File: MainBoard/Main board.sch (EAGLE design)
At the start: 9 parts

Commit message: Main board
Relabelled everything with power supply, labelled and redid traces.
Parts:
- removed POWER_SUPPLY_1, POWER_SUPPLY_3: (no value), pinhead:PINHD-2X3/90
- renumbered POWER_SUPPLY_2 to POWER_SUPPLY
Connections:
- net N$3 renamed POT_20
- net N$41 renamed POT_12
- net N$45 renamed POT_4
- removed net 5V: INSTRUMENT_1.1, INSTRUMENT_2.1, INSTRUMENT_3.1, POWER_SUPPLY.6, POWER_SUPPLY_1.6, POWER_SUPPLY_3.6
- removed net AUDIO_OUTPUT: 1/4"JACK.2, 1/4"JACK.4, 1/4"JACK.6, INSTRUMENT_1.20, INSTRUMENT_2.20, INSTRUMENT_3.20
- removed net N$1: INSTRUMENT_2.22
- removed net N$14: INSTRUMENT_1.22
- removed net N$18: INSTRUMENT_1.14, PATA_CABLE.37
- removed net N$2: INSTRUMENT_2.14, PATA_CABLE.36
- removed net N$31: PATA_CABLE.40
- removed net N$4: INSTRUMENT_3.22
- removed net N$5: INSTRUMENT_3.14, PATA_CABLE.39
- removed net N$52: INSTRUMENT_1.23
- removed net N$53: INSTRUMENT_1.24
- removed net N$54: INSTRUMENT_2.23
- removed net N$55: INSTRUMENT_2.24
- removed net N$56: INSTRUMENT_3.23
- removed net N$57: INSTRUMENT_3.24
- removed net N$58: POWER_SUPPLY_1.1
- removed net N$59: POWER_SUPPLY_1.3
- removed net N$60: POWER_SUPPLY_1.5
- removed net N$64: POWER_SUPPLY.1
- removed net N$65: POWER_SUPPLY.3
- removed net N$66: POWER_SUPPLY.5
- removed net N$7: INSTRUMENT_1.21
- removed net N$70: POWER_SUPPLY_3.1
- removed net N$71: POWER_SUPPLY_3.3
- removed net N$72: POWER_SUPPLY_3.5
- removed net N$8: INSTRUMENT_2.21
- removed net PETA_CABLE: INSTRUMENT_3.21
- new net +5V: INSTRUMENT_1.1, INSTRUMENT_2.1, INSTRUMENT_3.1, POWER_SUPPLY.6
- new net ANALOG_OUTPUT: 1/4"JACK.1, 1/4"JACK.3, 1/4"JACK.5, INSTRUMENT_1.20, INSTRUMENT_2.20, INSTRUMENT_3.20, MIXER_OUTPUT.1, MIXER_OUTPUT.3, MIXER_OUTPUT.5
- new net GND: MIXER_OUTPUT.6, PATA_CABLE.40
- new net POT_1: INSTRUMENT_1.5, PATA_CABLE.10
- new net POT_10: INSTRUMENT_2.6, PATA_CABLE.19
- new net POT_11: INSTRUMENT_2.7, PATA_CABLE.20
- new net POT_13: INSTRUMENT_2.9, PATA_CABLE.22
- new net POT_14: INSTRUMENT_2.10, PATA_CABLE.23
- new net POT_15: INSTRUMENT_2.11, PATA_CABLE.24
- new net POT_16: INSTRUMENT_2.12, PATA_CABLE.25
- new net POT_2: INSTRUMENT_1.6, PATA_CABLE.11
- new net POT_3: PATA_CABLE.12
- new net POT_5: PATA_CABLE.14
- new net POT_6: INSTRUMENT_1.10, PATA_CABLE.15
- new net POT_7: PATA_CABLE.16
- new net POT_8: INSTRUMENT_1.12, PATA_CABLE.17
- new net POT_9: INSTRUMENT_2.5, PATA_CABLE.18
- new net SWITCH_4: INSTRUMENT_2.16, PATA_CABLE.4
- new net SWITCH_5: INSTRUMENT_2.17, PATA_CABLE.5
- new net SWITCH_6: INSTRUMENT_2.19, PATA_CABLE.6
- new net SWITCH_7: INSTRUMENT_3.16, PATA_CABLE.7
- new net SWITCH_8: INSTRUMENT_3.17, PATA_CABLE.8
- new net SWITCH_9: INSTRUMENT_3.19, PATA_CABLE.9
- net +12V: no longer POWER_SUPPLY_1.2, POWER_SUPPLY_3.2
- net -12V: no longer POWER_SUPPLY_1.4, POWER_SUPPLY_3.4
- net ANALOG_GND: now also 1/4"JACK.2, 1/4"JACK.4, 1/4"JACK.6, INSTRUMENT_1.22, INSTRUMENT_2.22, INSTRUMENT_3.22, POWER_SUPPLY.1, POWER_SUPPLY.3; no longer 1/4"JACK.1, 1/4"JACK.3, 1/4"JACK.5
- net DIGITAL_GND: now also POWER_SUPPLY.5
- net POT_17: no longer INSTRUMENT_1.5, INSTRUMENT_2.5, PATA_CABLE.10, PATA_CABLE.18
- net POT_18: no longer INSTRUMENT_1.6, INSTRUMENT_2.6, PATA_CABLE.11, PATA_CABLE.19
- net POT_19: no longer INSTRUMENT_2.7, PATA_CABLE.12, PATA_CABLE.20
- net POT_21: no longer INSTRUMENT_2.9, PATA_CABLE.14, PATA_CABLE.22
- net POT_22: no longer INSTRUMENT_1.10, INSTRUMENT_2.10, PATA_CABLE.15, PATA_CABLE.23
- net POT_23: no longer INSTRUMENT_2.11, PATA_CABLE.16, PATA_CABLE.24
- net POT_24: no longer INSTRUMENT_1.12, INSTRUMENT_2.12, PATA_CABLE.17, PATA_CABLE.25
- net SWITCH_1: no longer INSTRUMENT_2.16, INSTRUMENT_3.16, PATA_CABLE.4, PATA_CABLE.7
- net SWITCH_2: no longer INSTRUMENT_2.17, INSTRUMENT_3.17, PATA_CABLE.5, PATA_CABLE.8
- net SWITCH_3: no longer INSTRUMENT_2.19, INSTRUMENT_3.19, PATA_CABLE.6, PATA_CABLE.9
- net TO_POT_PCB: now also INSTRUMENT_1.14, INSTRUMENT_2.14, INSTRUMENT_3.14, PATA_CABLE.36, PATA_CABLE.37, PATA_CABLE.39
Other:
- note removed: "+12V_INPUT"
- note removed: "+12V_OUTPUT"
- note removed: "-12V_INPUT"
- note removed: "-12V_OUTPUT"
- note removed: "5V_INPUT"
- note removed: "5V_OUTPUT"
- note removed: "GND"
- note removed: "POT_1"
- note removed: "POT_10"
- note removed: "POT_11"
- note removed: "POT_12"
- note removed: "POT_13"
- note removed: "POT_14"
- note removed: "POT_15"
- note removed: "POT_16"
- note removed: "POT_2"
- note removed: "POT_20"
- note removed: "POT_3"
- note removed: "POT_4"
- note removed: "POT_5"
- note removed: "POT_6"
- note removed: "POT_7"
- note removed: "POT_8"
- note removed: "POT_9"
- note removed: "SWITCH_1"
- note removed: "SWITCH_2"
- note removed: "SWITCH_3"
- note removed: "SWITCH_4"
- note removed: "SWITCH_5"
- note removed: "SWITCH_6"
- note removed: "SWITCH_7"
- note removed: "SWITCH_8"
- note removed: "SWITCH_9"
- note removed: "TO_POT_PCB"
- moved on the sheet: 1/4"JACK, INSTRUMENT_2, INSTRUMENT_3, MIXER_OUTPUT

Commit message: Version 2 of mainboard
Corrected lots of thingamajics.
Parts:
- added POWER_SUPPLY_PINOUT_1, POWER_SUPPLY_PINOUT_2: (no value), pinhead:PINHD-2X3
- 1/4"JACK, MIXER_OUTPUT: device pinhead:PINHD-2X3/90 -> pinhead:PINHD-2X3
- INSTRUMENT_1, INSTRUMENT_2, INSTRUMENT_3: device pinhead:PINHD-2X12/90 -> pinhead:PINHD-2X12
- PATA_CABLE: device pinhead:PINHD-2X20/90 -> pinhead:PINHD-2X20
- POWER_SUPPLY: value (none) -> TER6PIN_VERT; device pinhead:PINHD-2X3/90 -> TE6Pin:TER6PIN_VERT
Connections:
- net POT_1 renamed POT_1A
- net POT_10 renamed POT_5B
- net POT_11 renamed POT_6A
- net POT_12 renamed POT_6B
- net POT_13 renamed POT_7A
- net POT_14 renamed POT_7B
- net POT_15 renamed POT_8A
- net POT_16 renamed POT_8B
- net POT_17 renamed POT_9A
- net POT_18 renamed POT_9B
- net POT_2 renamed POT_1B
- net POT_20 renamed POT_10B
- net POT_22 renamed POT_11B
- net POT_24 renamed POT_12B
- net POT_4 renamed POT_2B
- net POT_6 renamed POT_3B
- net POT_8 renamed POT_4B
- net POT_9 renamed POT_5A
- removed net ANALOG_OUTPUT: 1/4"JACK.1, 1/4"JACK.3, 1/4"JACK.5, INSTRUMENT_1.20, INSTRUMENT_2.20, INSTRUMENT_3.20, MIXER_OUTPUT.1, MIXER_OUTPUT.3, MIXER_OUTPUT.5
- removed net POT_19: INSTRUMENT_1.7, INSTRUMENT_3.7, PATA_CABLE.28
- removed net POT_21: INSTRUMENT_1.9, INSTRUMENT_3.9, PATA_CABLE.30
- removed net POT_23: INSTRUMENT_1.11, INSTRUMENT_3.11, PATA_CABLE.32
- removed net POT_3: PATA_CABLE.12
- removed net POT_5: PATA_CABLE.14
- removed net POT_7: PATA_CABLE.16
- new net ANALOG_OUTPUT_1: 1/4"JACK.1, INSTRUMENT_1.20, MIXER_OUTPUT.1
- new net ANALOG_OUTPUT_2: 1/4"JACK.3, INSTRUMENT_2.20, MIXER_OUTPUT.3
- new net ANALOG_OUTPUT_3: 1/4"JACK.5, INSTRUMENT_3.20, MIXER_OUTPUT.5
- new net POT_10A: INSTRUMENT_3.7, PATA_CABLE.28
- new net POT_11A: INSTRUMENT_1.9, INSTRUMENT_3.9, PATA_CABLE.14, PATA_CABLE.30
- new net POT_12A: INSTRUMENT_1.11, INSTRUMENT_3.11, PATA_CABLE.16, PATA_CABLE.32
- new net POT_2A: INSTRUMENT_1.7, PATA_CABLE.12
- net +12V: now also POWER_SUPPLY.+12V, POWER_SUPPLY_PINOUT_1.1, POWER_SUPPLY_PINOUT_2.1; no longer POWER_SUPPLY.2
- net +5V: now also POWER_SUPPLY.+5V, POWER_SUPPLY_PINOUT_1.5, POWER_SUPPLY_PINOUT_2.5; no longer POWER_SUPPLY.6
- net -12V: now also POWER_SUPPLY.-12V, POWER_SUPPLY_PINOUT_1.3, POWER_SUPPLY_PINOUT_2.3; no longer POWER_SUPPLY.4
- net ANALOG_GND: now also POWER_SUPPLY.AGND0, POWER_SUPPLY.AGND1, POWER_SUPPLY_PINOUT_1.2, POWER_SUPPLY_PINOUT_2.2; no longer POWER_SUPPLY.1, POWER_SUPPLY.3
- net DIGITAL_GND: now also POWER_SUPPLY.DGND, POWER_SUPPLY_PINOUT_1.4, POWER_SUPPLY_PINOUT_2.4; no longer POWER_SUPPLY.5
- net GND: now also POWER_SUPPLY_PINOUT_1.6, POWER_SUPPLY_PINOUT_2.6
- net TO_POT_PCB: no longer PATA_CABLE.35, PATA_CABLE.37, PATA_CABLE.39
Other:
- note added: "POWER_SUPPLY"
- moved on the sheet: INSTRUMENT_2, INSTRUMENT_3

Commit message: Finished layout - needs silk screen
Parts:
- added SV1: (no value), con-lstb:MA03-2
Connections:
- net ANALOG_OUTPUT_1 renamed OUT1
- net ANALOG_OUTPUT_2 renamed OUT2
- net ANALOG_OUTPUT_3 renamed OUT3
- removed net ANALOG_GND: 1/4"JACK.2, 1/4"JACK.4, 1/4"JACK.6, INSTRUMENT_1.18, INSTRUMENT_1.22, INSTRUMENT_2.18, INSTRUMENT_2.22, INSTRUMENT_3.18, INSTRUMENT_3.22, POWER_SUPPLY.AGND0, POWER_SUPPLY.AGND1, POWER_SUPPLY_PINOUT_1.2, POWER_SUPPLY_PINOUT_2.2
- removed net DIGITAL_GND: INSTRUMENT_1.3, INSTRUMENT_2.3, INSTRUMENT_3.3, POWER_SUPPLY.DGND, POWER_SUPPLY_PINOUT_1.4, POWER_SUPPLY_PINOUT_2.4
- removed net GND: MIXER_OUTPUT.6, PATA_CABLE.40, POWER_SUPPLY_PINOUT_1.6, POWER_SUPPLY_PINOUT_2.6
- removed net SEQUENCER_TRIGGER: INSTRUMENT_1.15, INSTRUMENT_2.15, INSTRUMENT_3.15
- removed net SWITCH_2: INSTRUMENT_1.17, PATA_CABLE.2
- removed net SWITCH_3: INSTRUMENT_1.19, PATA_CABLE.3
- removed net SWITCH_4: INSTRUMENT_2.16, PATA_CABLE.4
- removed net SWITCH_5: INSTRUMENT_2.17, PATA_CABLE.5
- removed net SWITCH_6: INSTRUMENT_2.19, PATA_CABLE.6
- removed net SWITCH_7: INSTRUMENT_3.16, PATA_CABLE.7
- removed net SWITCH_8: INSTRUMENT_3.17, PATA_CABLE.8
- removed net SWITCH_9: INSTRUMENT_3.19, PATA_CABLE.9
- removed net TO_POT_PCB: INSTRUMENT_1.13, INSTRUMENT_1.14, INSTRUMENT_2.13, INSTRUMENT_2.14, INSTRUMENT_3.13, INSTRUMENT_3.14, PATA_CABLE.34, PATA_CABLE.36, PATA_CABLE.38
- new net AGND: 1/4"JACK.2, 1/4"JACK.4, 1/4"JACK.6, INSTRUMENT_1.18, INSTRUMENT_1.22, INSTRUMENT_2.18, INSTRUMENT_2.22, INSTRUMENT_3.18, INSTRUMENT_3.22, MIXER_OUTPUT.2, MIXER_OUTPUT.4, MIXER_OUTPUT.6, PATA_CABLE.40, POWER_SUPPLY.AGND0, POWER_SUPPLY.AGND1, POWER_SUPPLY_PINOUT_1.2, POWER_SUPPLY_PINOUT_1.4, POWER_SUPPLY_PINOUT_2.2, POWER_SUPPLY_PINOUT_2.4
- new net DGND: INSTRUMENT_1.3, INSTRUMENT_2.3, INSTRUMENT_3.3, POWER_SUPPLY.DGND, POWER_SUPPLY_PINOUT_1.6, POWER_SUPPLY_PINOUT_2.6
- new net POT_13A: INSTRUMENT_3.9, PATA_CABLE.31
- new net POT_13B: INSTRUMENT_3.10, PATA_CABLE.32
- new net POT_14A: INSTRUMENT_3.11, PATA_CABLE.33
- new net POT_14B: INSTRUMENT_3.12, PATA_CABLE.34
- new net POT_15A: INSTRUMENT_3.13, PATA_CABLE.35
- new net POT_15B: INSTRUMENT_3.14, PATA_CABLE.36
- new net POT_3A: INSTRUMENT_1.9, PATA_CABLE.5
- new net POT_4A: INSTRUMENT_1.11, PATA_CABLE.7
- new net SW_2: INSTRUMENT_1.17, PATA_CABLE.11
- new net SW_3: INSTRUMENT_1.19, PATA_CABLE.13
- new net SW_4: INSTRUMENT_2.16, PATA_CABLE.25
- new net SW_5: INSTRUMENT_2.17, PATA_CABLE.24
- new net SW_6: INSTRUMENT_2.19, PATA_CABLE.26
- new net SW_7: INSTRUMENT_3.16, PATA_CABLE.38
- new net SW_8: INSTRUMENT_3.17, PATA_CABLE.37
- new net SW_9: INSTRUMENT_3.19, PATA_CABLE.39
- new net TRIG1: INSTRUMENT_1.15, SV1.5, SV1.6
- new net TRIG2: INSTRUMENT_2.15, SV1.3, SV1.4
- new net TRIG3: INSTRUMENT_3.15, SV1.1, SV1.2
- net POT_10A: now also INSTRUMENT_2.13, PATA_CABLE.22; no longer INSTRUMENT_3.7, PATA_CABLE.28
- net POT_10B: now also INSTRUMENT_2.14, PATA_CABLE.23; no longer INSTRUMENT_3.8, PATA_CABLE.29
- net POT_11A: now also INSTRUMENT_3.5, PATA_CABLE.27; no longer INSTRUMENT_1.9, INSTRUMENT_3.9, PATA_CABLE.14, PATA_CABLE.30
- net POT_11B: now also INSTRUMENT_3.6, PATA_CABLE.28; no longer INSTRUMENT_3.10, PATA_CABLE.31
- net POT_12A: now also INSTRUMENT_3.7, PATA_CABLE.29; no longer INSTRUMENT_1.11, INSTRUMENT_3.11, PATA_CABLE.16, PATA_CABLE.32
- net POT_12B: now also INSTRUMENT_3.8, PATA_CABLE.30; no longer INSTRUMENT_3.12, PATA_CABLE.33
- net POT_1A: now also PATA_CABLE.1; no longer PATA_CABLE.10
- net POT_1B: now also PATA_CABLE.2; no longer PATA_CABLE.11
- net POT_2A: now also PATA_CABLE.3; no longer PATA_CABLE.12
- net POT_2B: now also PATA_CABLE.4; no longer PATA_CABLE.13
- net POT_3B: now also PATA_CABLE.6; no longer PATA_CABLE.15
- net POT_4B: now also PATA_CABLE.8; no longer PATA_CABLE.17
- net POT_5A: now also INSTRUMENT_1.13, PATA_CABLE.9; no longer INSTRUMENT_2.5, PATA_CABLE.18
- net POT_5B: now also INSTRUMENT_1.14, PATA_CABLE.10; no longer INSTRUMENT_2.6, PATA_CABLE.19
- net POT_6A: now also INSTRUMENT_2.5, PATA_CABLE.14; no longer INSTRUMENT_2.7, PATA_CABLE.20
- net POT_6B: now also INSTRUMENT_2.6, PATA_CABLE.15; no longer INSTRUMENT_2.8, PATA_CABLE.21
- net POT_7A: now also INSTRUMENT_2.7, PATA_CABLE.16; no longer INSTRUMENT_2.9, PATA_CABLE.22
- net POT_7B: now also INSTRUMENT_2.8, PATA_CABLE.17; no longer INSTRUMENT_2.10, PATA_CABLE.23
- net POT_8A: now also INSTRUMENT_2.9, PATA_CABLE.18; no longer INSTRUMENT_2.11, PATA_CABLE.24
- net POT_8B: now also INSTRUMENT_2.10, PATA_CABLE.19; no longer INSTRUMENT_2.12, PATA_CABLE.25
- net POT_9A: now also INSTRUMENT_2.11, PATA_CABLE.20; no longer INSTRUMENT_3.5, PATA_CABLE.26
- net POT_9B: now also INSTRUMENT_2.12, PATA_CABLE.21; no longer INSTRUMENT_3.6, PATA_CABLE.27
- net SWITCH_1: now also PATA_CABLE.12; no longer PATA_CABLE.1
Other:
- moved on the sheet: INSTRUMENT_2, INSTRUMENT_3

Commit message: Version 3 of mainboard
Added sequencer pinouts and manually did all traces.
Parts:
- removed SV1: (no value), con-lstb:MA03-2
- added SEQUENCER_OUTPUT: (no value), pinhead:PINHD-2X3
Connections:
- net DGND renamed DIGITAL_GND
- net OUT1 renamed ANALOG_OUTPUT_1
- net OUT2 renamed ANALOG_OUTPUT_2
- net OUT3 renamed ANALOG_OUTPUT_3
- net SW_2 renamed SWITCH_2
- net SW_3 renamed SWITCH_3
- net SW_4 renamed SWITCH_4
- net SW_5 renamed SWITCH_5
- net SW_6 renamed SWITCH_6
- net SW_7 renamed SWITCH_7
- net SW_8 renamed SWITCH_8
- net SW_9 renamed SWITCH_9
- removed net AGND: 1/4"JACK.2, 1/4"JACK.4, 1/4"JACK.6, INSTRUMENT_1.18, INSTRUMENT_1.22, INSTRUMENT_2.18, INSTRUMENT_2.22, INSTRUMENT_3.18, INSTRUMENT_3.22, MIXER_OUTPUT.2, MIXER_OUTPUT.4, MIXER_OUTPUT.6, PATA_CABLE.40, POWER_SUPPLY.AGND0, POWER_SUPPLY.AGND1, POWER_SUPPLY_PINOUT_1.2, POWER_SUPPLY_PINOUT_1.4, POWER_SUPPLY_PINOUT_2.2, POWER_SUPPLY_PINOUT_2.4
- removed net TRIG1: INSTRUMENT_1.15, SV1.5, SV1.6
- removed net TRIG2: INSTRUMENT_2.15, SV1.3, SV1.4
- removed net TRIG3: INSTRUMENT_3.15, SV1.1, SV1.2
- new net ANALOG_GND: 1/4"JACK.2, 1/4"JACK.4, 1/4"JACK.6, INSTRUMENT_1.18, INSTRUMENT_1.22, INSTRUMENT_2.18, INSTRUMENT_2.22, INSTRUMENT_3.18, INSTRUMENT_3.22, POWER_SUPPLY.AGND0, POWER_SUPPLY.AGND1, POWER_SUPPLY_PINOUT_1.2, POWER_SUPPLY_PINOUT_1.4, POWER_SUPPLY_PINOUT_2.2, POWER_SUPPLY_PINOUT_2.4, SEQUENCER_OUTPUT.2, SEQUENCER_OUTPUT.4, SEQUENCER_OUTPUT.6
- new net GND: MIXER_OUTPUT.6
- new net N$1: SEQUENCER_OUTPUT.3
- new net SEQUENCER_TRIGGER: INSTRUMENT_1.15, INSTRUMENT_2.15, INSTRUMENT_3.15, SEQUENCER_OUTPUT.1, SEQUENCER_OUTPUT.5
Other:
- moved on the sheet: INSTRUMENT_2, INSTRUMENT_3

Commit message: This board should work
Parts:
- removed SEQUENCER_OUTPUT: (no value), pinhead:PINHD-2X3
- added TRIG_IN: (no value), con-lstb:MA03-2
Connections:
- net ANALOG_OUTPUT_1 renamed OUT1
- net ANALOG_OUTPUT_2 renamed OUT2
- net ANALOG_OUTPUT_3 renamed OUT3
- net DIGITAL_GND renamed DGND
- net SWITCH_2 renamed SW_2
- net SWITCH_3 renamed SW_3
- net SWITCH_4 renamed SW_4
- net SWITCH_5 renamed SW_5
- net SWITCH_6 renamed SW_6
- net SWITCH_7 renamed SW_7
- net SWITCH_8 renamed SW_8
- net SWITCH_9 renamed SW_9
- removed net ANALOG_GND: 1/4"JACK.2, 1/4"JACK.4, 1/4"JACK.6, INSTRUMENT_1.18, INSTRUMENT_1.22, INSTRUMENT_2.18, INSTRUMENT_2.22, INSTRUMENT_3.18, INSTRUMENT_3.22, POWER_SUPPLY.AGND0, POWER_SUPPLY.AGND1, POWER_SUPPLY_PINOUT_1.2, POWER_SUPPLY_PINOUT_1.4, POWER_SUPPLY_PINOUT_2.2, POWER_SUPPLY_PINOUT_2.4, SEQUENCER_OUTPUT.2, SEQUENCER_OUTPUT.4, SEQUENCER_OUTPUT.6
- removed net GND: MIXER_OUTPUT.6
- removed net N$1: SEQUENCER_OUTPUT.3
- removed net SEQUENCER_TRIGGER: INSTRUMENT_1.15, INSTRUMENT_2.15, INSTRUMENT_3.15, SEQUENCER_OUTPUT.1, SEQUENCER_OUTPUT.5
- new net AGND: 1/4"JACK.2, 1/4"JACK.4, 1/4"JACK.6, INSTRUMENT_1.18, INSTRUMENT_1.22, INSTRUMENT_2.18, INSTRUMENT_2.22, INSTRUMENT_3.18, INSTRUMENT_3.22, MIXER_OUTPUT.2, MIXER_OUTPUT.4, MIXER_OUTPUT.6, PATA_CABLE.40, POWER_SUPPLY.AGND0, POWER_SUPPLY.AGND1, POWER_SUPPLY_PINOUT_1.2, POWER_SUPPLY_PINOUT_1.4, POWER_SUPPLY_PINOUT_2.2, POWER_SUPPLY_PINOUT_2.4
- new net TRIG1: INSTRUMENT_1.15, TRIG_IN.5, TRIG_IN.6
- new net TRIG2: INSTRUMENT_2.15, TRIG_IN.3, TRIG_IN.4
- new net TRIG3: INSTRUMENT_3.15, TRIG_IN.1, TRIG_IN.2
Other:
- moved on the sheet: INSTRUMENT_2, INSTRUMENT_3

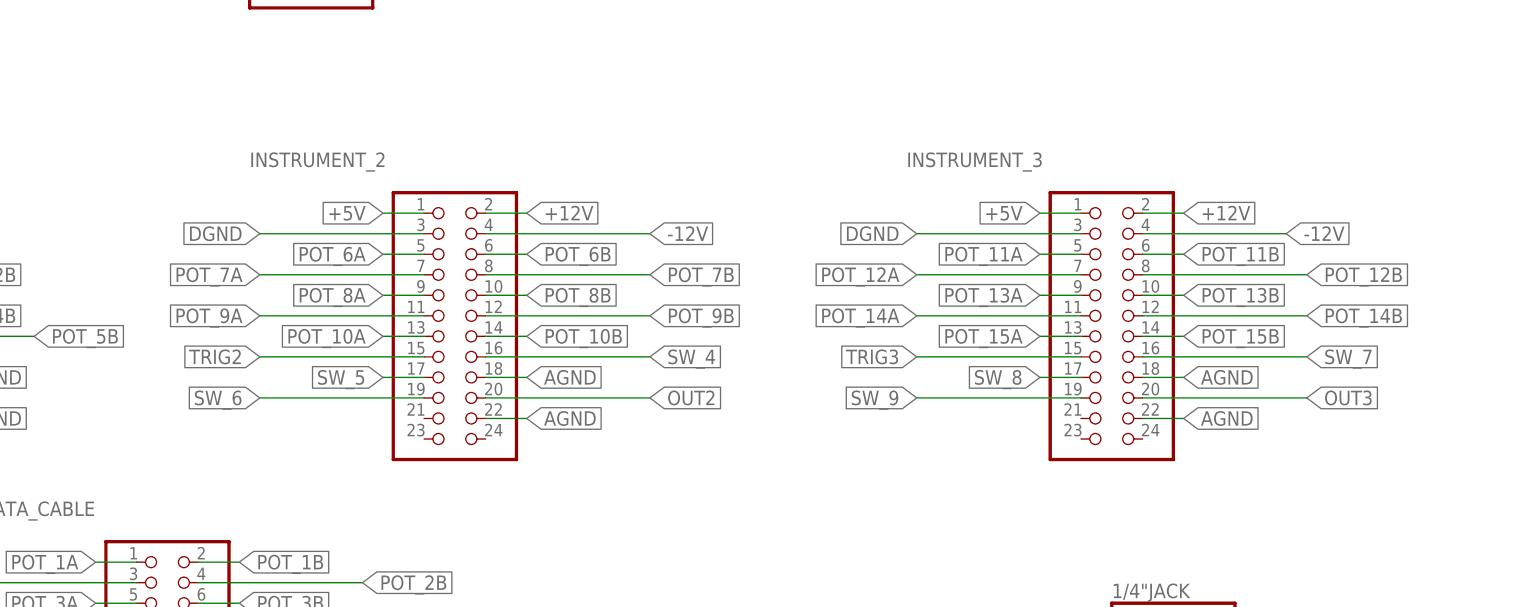
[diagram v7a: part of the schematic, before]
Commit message: Swapped Instruments 2 and 3
Swapped instruments 2 and 3 so they are in proper order
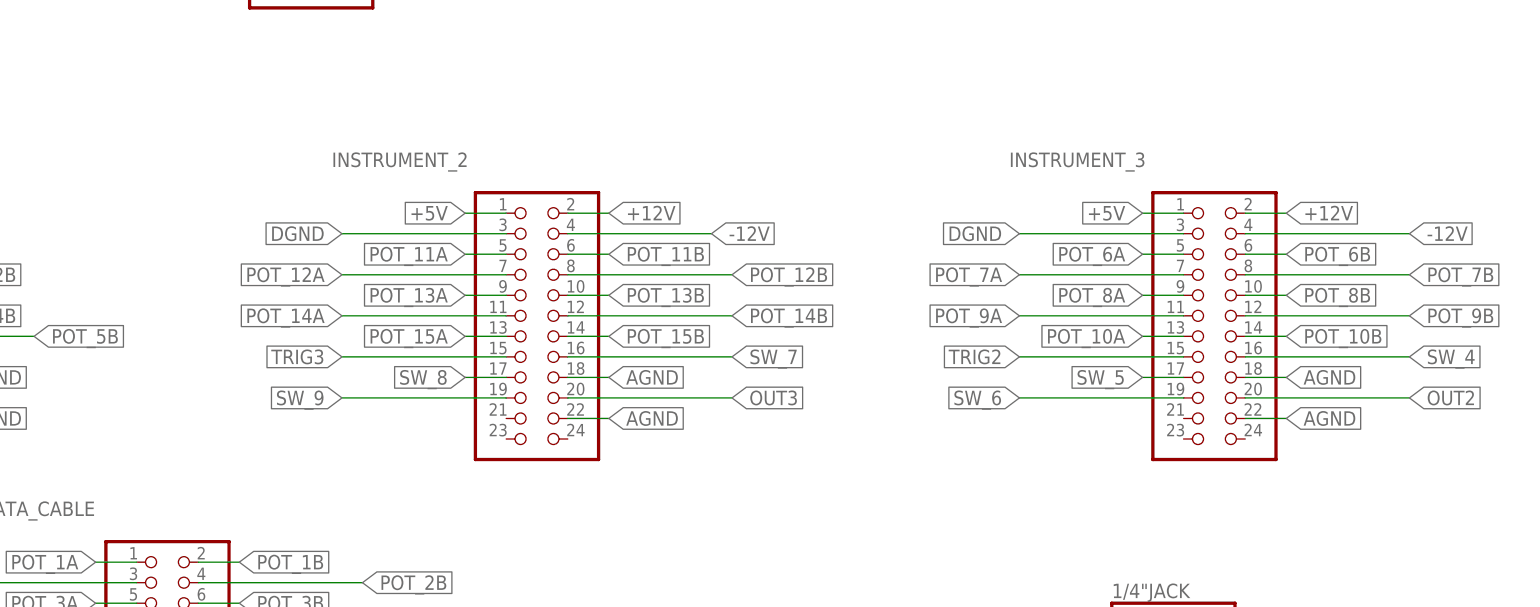
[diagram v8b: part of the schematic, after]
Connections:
- net OUT2: now also INSTRUMENT_3.20; no longer INSTRUMENT_2.20
- net OUT3: now also INSTRUMENT_2.20; no longer INSTRUMENT_3.20
- net POT_10A: now also INSTRUMENT_3.13; no longer INSTRUMENT_2.13
- net POT_10B: now also INSTRUMENT_3.14; no longer INSTRUMENT_2.14
- net POT_11A: now also INSTRUMENT_2.5; no longer INSTRUMENT_3.5
- net POT_11B: now also INSTRUMENT_2.6; no longer INSTRUMENT_3.6
- net POT_12A: now also INSTRUMENT_2.7; no longer INSTRUMENT_3.7
- net POT_12B: now also INSTRUMENT_2.8; no longer INSTRUMENT_3.8
- net POT_13A: now also INSTRUMENT_2.9; no longer INSTRUMENT_3.9
- net POT_13B: now also INSTRUMENT_2.10; no longer INSTRUMENT_3.10
- net POT_14A: now also INSTRUMENT_2.11; no longer INSTRUMENT_3.11
- net POT_14B: now also INSTRUMENT_2.12; no longer INSTRUMENT_3.12
- net POT_15A: now also INSTRUMENT_2.13; no longer INSTRUMENT_3.13
- net POT_15B: now also INSTRUMENT_2.14; no longer INSTRUMENT_3.14
- net POT_6A: now also INSTRUMENT_3.5; no longer INSTRUMENT_2.5
- net POT_6B: now also INSTRUMENT_3.6; no longer INSTRUMENT_2.6
- net POT_7A: now also INSTRUMENT_3.7; no longer INSTRUMENT_2.7
- net POT_7B: now also INSTRUMENT_3.8; no longer INSTRUMENT_2.8
- net POT_8A: now also INSTRUMENT_3.9; no longer INSTRUMENT_2.9
- net POT_8B: now also INSTRUMENT_3.10; no longer INSTRUMENT_2.10
- net POT_9A: now also INSTRUMENT_3.11; no longer INSTRUMENT_2.11
- net POT_9B: now also INSTRUMENT_3.12; no longer INSTRUMENT_2.12
- net SW_4: now also INSTRUMENT_3.16; no longer INSTRUMENT_2.16
- net SW_5: now also INSTRUMENT_3.17; no longer INSTRUMENT_2.17
- net SW_6: now also INSTRUMENT_3.19; no longer INSTRUMENT_2.19
- net SW_7: now also INSTRUMENT_2.16; no longer INSTRUMENT_3.16
- net SW_8: now also INSTRUMENT_2.17; no longer INSTRUMENT_3.17
- net SW_9: now also INSTRUMENT_2.19; no longer INSTRUMENT_3.19
- net TRIG2: now also INSTRUMENT_3.15; no longer INSTRUMENT_2.15
- net TRIG3: now also INSTRUMENT_2.15; no longer INSTRUMENT_3.15
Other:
- moved on the sheet: INSTRUMENT_2, INSTRUMENT_3
